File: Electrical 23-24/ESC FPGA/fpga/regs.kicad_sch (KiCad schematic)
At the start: 71 parts, among them SW1 SW_SPDT, U12 MIC28515T-E/PHA, U6 MIC28515T-E/PHA, U7 MIC28515T-E/PHA, U8 LM74700QDBVRQ1, U9 LM74700QDBVRQ1

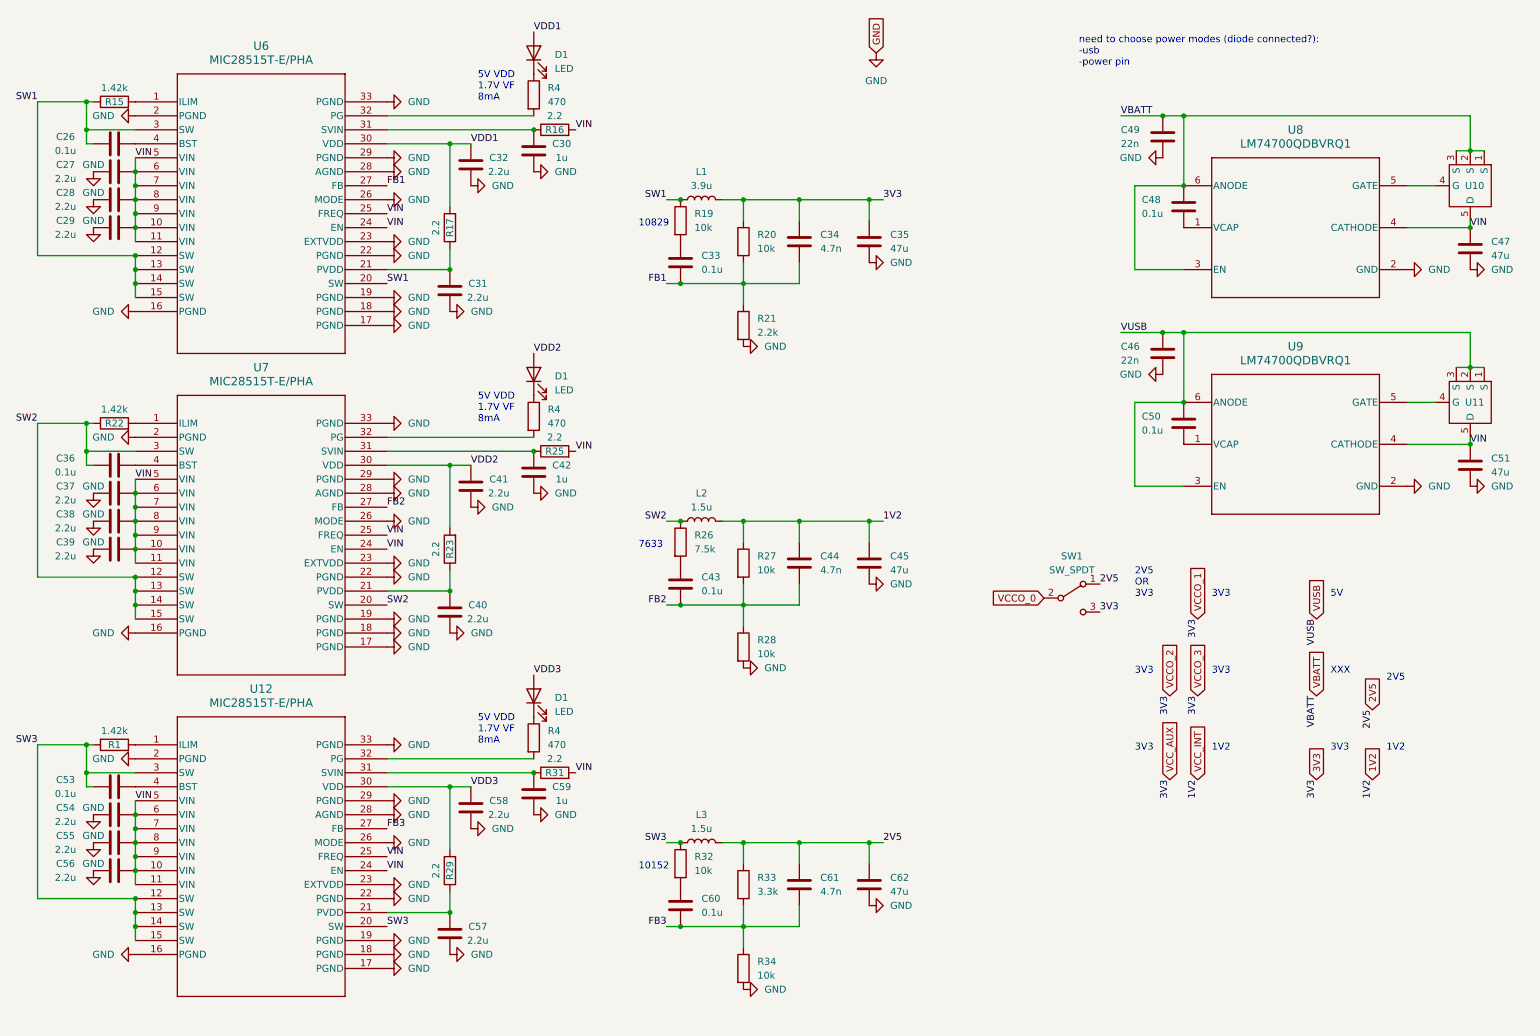
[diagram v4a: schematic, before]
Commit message: Made BOM, need to modify footprints
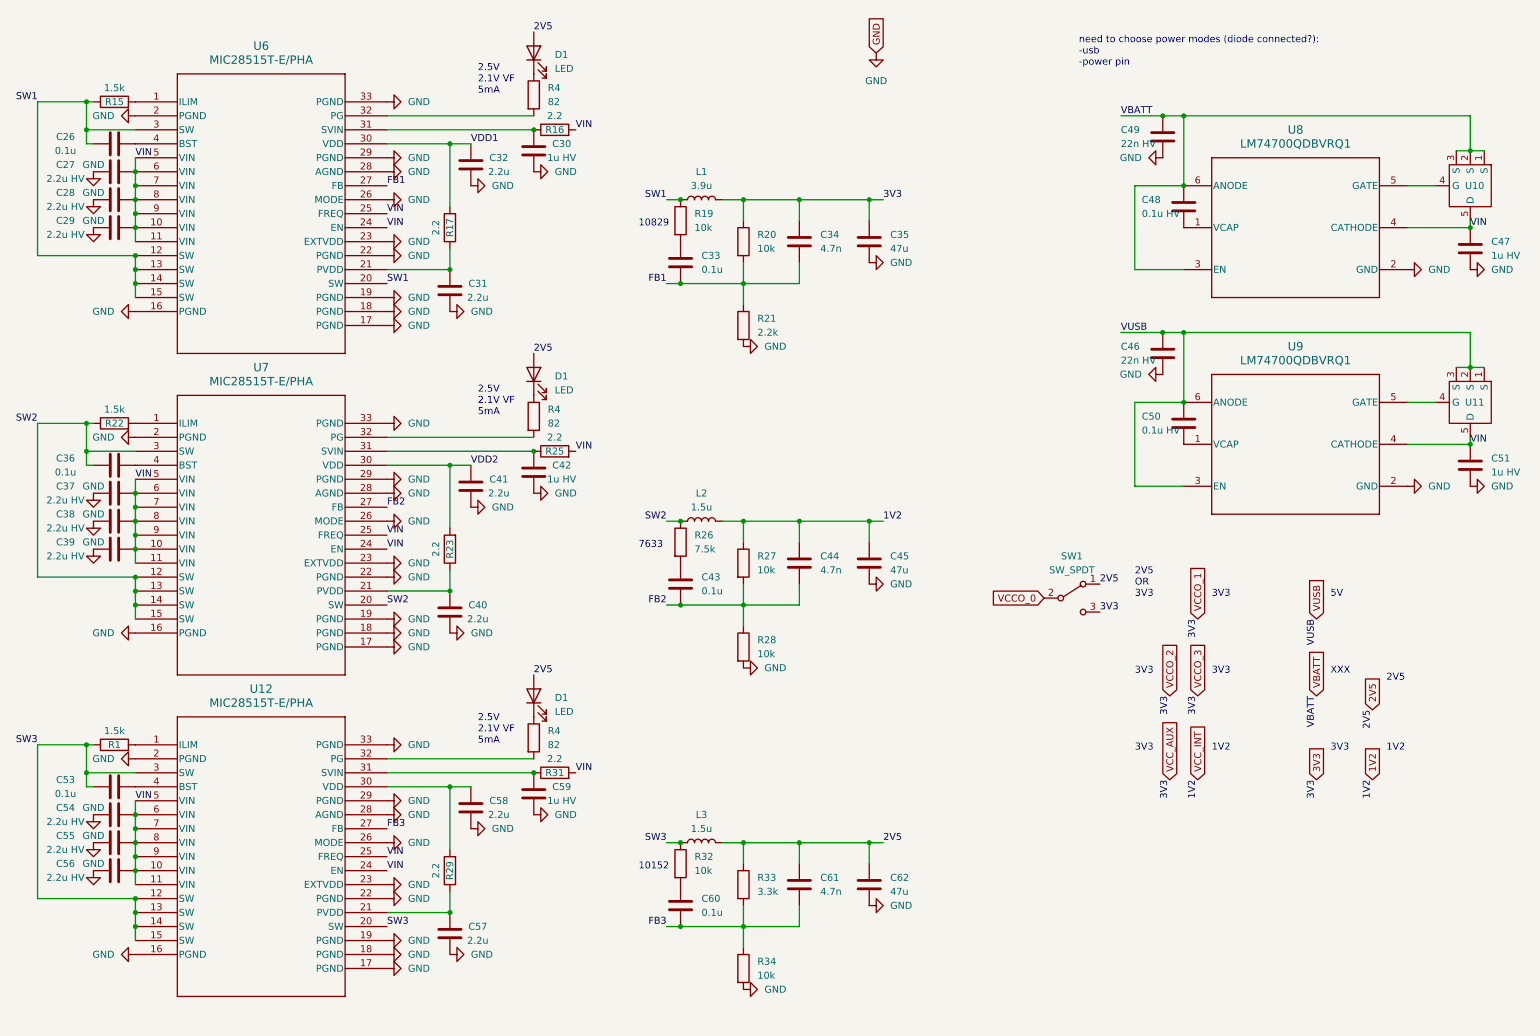
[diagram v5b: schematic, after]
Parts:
- removed D1 (x2): LED, symbol Device:LED
- added D1 (x2): LED, LED_SMD:LED_0805_2012Metric_Pad1.15x1.40mm_HandSolder, symbol Device:LED
- C26, C31, C32, C33, C34, C35, C36, C40, C41, C43, C44, C45, C53, C57, C58, C60, C61, C62: footprint (none) -> Capacitor_SMD:C_0402_1005Metric_Pad0.74x0.62mm_HandSolder
- C27, C28, C29, C37, C38, C39, C54, C55, C56: value 2.2u -> 2.2u HV; footprint (none) -> Capacitor_SMD:C_0402_1005Metric_Pad0.74x0.62mm_HandSolder
- C30, C42, C59: value 1u -> 1u HV; footprint (none) -> Capacitor_SMD:C_0402_1005Metric_Pad0.74x0.62mm_HandSolder
- C46, C49: value 22n -> 22n HV; footprint (none) -> Capacitor_SMD:C_0402_1005Metric_Pad0.74x0.62mm_HandSolder
- C47, C51: value 47u -> 1u HV; footprint (none) -> Capacitor_SMD:C_0402_1005Metric_Pad0.74x0.62mm_HandSolder
- C48, C50: value 0.1u -> 0.1u HV; footprint (none) -> Capacitor_SMD:C_0402_1005Metric_Pad0.74x0.62mm_HandSolder
- D1: footprint (none) -> LED_SMD:LED_0805_2012Metric_Pad1.15x1.40mm_HandSolder; Digi (none) -> https://www.digikey.com/en/products/detail/harvatek-corpora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
- L1, L2, L3: footprint (none) -> Inductor_SMD:L_0402_1005Metric_Pad0.77x0.64mm_HandSolder
- R1, R15, R22: value 1.42k -> 1.5k; footprint (none) -> Resistor_SMD:R_0402_1005Metric_Pad0.72x0.64mm_HandSolder
- R16, R17, R19, R20, R21, R23, R25, R26, R27, R28, R29, R31, R32, R33, R34: footprint (none) -> Resistor_SMD:R_0402_1005Metric_Pad0.72x0.64mm_HandSolder
- R4: value 470 -> 82; footprint (none) -> Resistor_SMD:R_0402_1005Metric_Pad0.72x0.64mm_HandSolder
- SW1: footprint (none) -> Connector_PinHeader_2.54mm:PinHeader_1x03_P2.54mm_Vertical; Digi (none) -> https://www.digikey.com/en/products/detail/cui-devices/SLW-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
- U12, U6, U7: footprint VQFN32_PHA_MCH -> fpga:VQFN32_PHA_MCH
- U8, U9: footprint DBV0006A_N -> fpga:DBV0006A_N
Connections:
- net 2V5: now also D1.2 (A), D1.2 (A), D1.2 (A)
- net at R4.1: now also D1.1 (K) (x2)
- net VDD3: no longer names the net of C58.2, R29.2, U12.30 (VDD)
- net VDD3: no longer D1.2 (A)
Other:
- note added: "2.5V 2.1V VF 5mA"
- note removed: "5V VDD 1.7V VF 8mA"

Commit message: Finish groupings on FPGA PCB
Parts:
- added JP1, JP2, JP3, JP4, JP5, JP6, JP7, JP8, JP9: SolderJumper_2_Bridged, Jumper:SolderJumper-2_P1.3mm_Bridged2Bar_RoundedPad1.0x1.5mm, symbol Jumper:SolderJumper_2_Bridged
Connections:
- net 1V2: now also JP7.1 (A)
- net 3V3: now also JP4.1 (A), JP5.1 (A), JP6.1 (A), JP8.1 (A)
- net GND: now also JP1.2 (B), JP2.2 (B), JP3.2 (B); no longer C32.1, C35.2, C41.1, C45.2, C58.1, C62.2, R21.2, R28.2, R34.2, U12.28 (AGND), U6.28 (AGND), U7.28 (AGND)
- net VCCO_0: now also JP9.1 (A); no longer SW1.2 (B)
- new net: JP9.2 (B), SW1.2 (B)
- new net GNDA: C32.1, C35.2, C41.1, C45.2, C58.1, C62.2, JP1.1 (A), JP2.1 (A), JP3.1 (A), R21.2, R28.2, R34.2, U12.28 (AGND), U6.28 (AGND), U7.28 (AGND)
- new net VCCO_1: JP4.2 (B)
- new net VCCO_2: JP6.2 (B)
- new net VCCO_3: JP5.2 (B)
- new net VCC_AUX: JP8.2 (B)
- new net VCC_INT: JP7.2 (B)
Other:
- note added: "ADD TESTPOINT"

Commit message: Turn XT60
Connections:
- removed net GNDA: C32.1, C35.2, C41.1, C45.2, C58.1, C62.2, JP1.1 (A), JP2.1 (A), JP3.1 (A), R21.2, R28.2, R34.2, U12.28 (AGND), U6.28 (AGND), U7.28 (AGND)
- new net GND1: C32.1, C35.2, JP1.1 (A), R21.2, U6.28 (AGND)
- new net GND2: C41.1, C45.2, JP2.1 (A), R28.2, U7.28 (AGND)
- new net GND3: C58.1, C62.2, JP3.1 (A), R34.2, U12.28 (AGND)
